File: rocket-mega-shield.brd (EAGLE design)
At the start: 114.3 x 60 mm, 57 parts

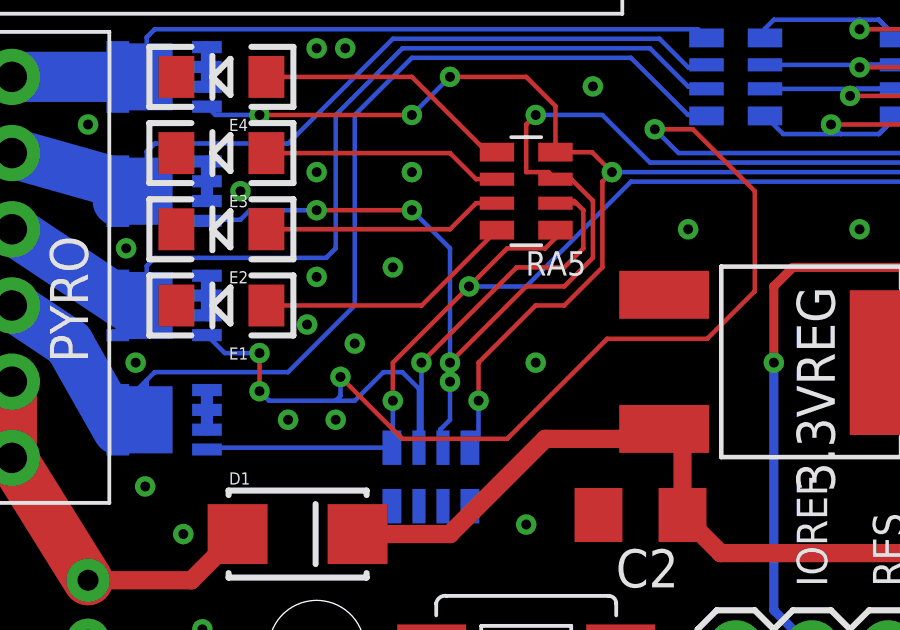
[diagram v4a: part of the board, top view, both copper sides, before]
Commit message: fixing goofy extra via
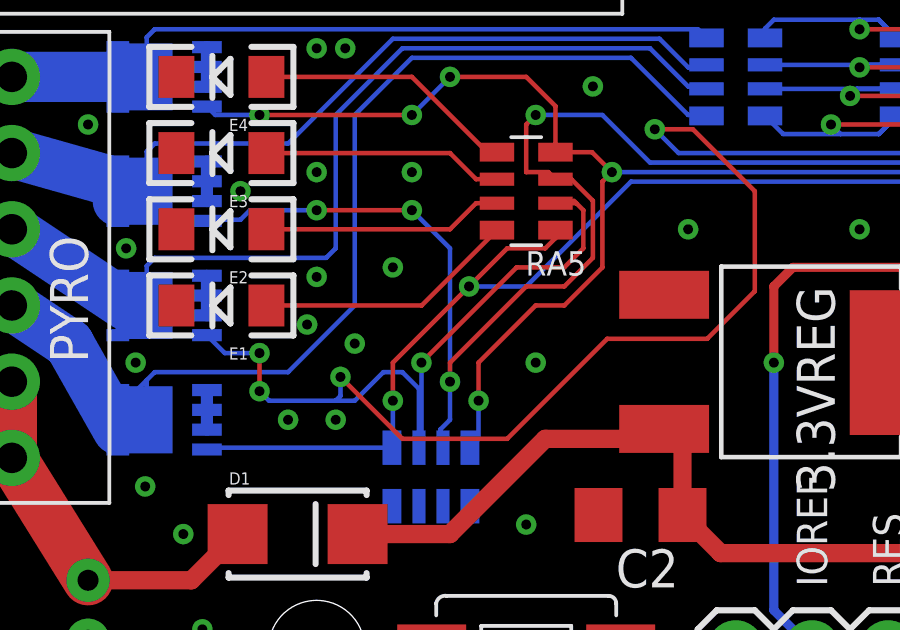
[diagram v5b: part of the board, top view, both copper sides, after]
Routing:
- net PYRO3: track 102.4 -> 103.0 mm, vias 5 -> 4
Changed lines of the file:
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@@
 <wire x1="26.9875" y1="13.6525" x2="26.9875" y2="13.1215" width="0.1524" layer="16"/>
 <wire x1="26.9875" y1="13.1215" x2="27.07" y2="13.039" width="0.1524" layer="16"/>
-<via x="27.305" y="15.875" extent="1-16" drill="0.3302"/>
-<wire x1="27.305" y1="15.875" x2="27.305" y2="19.685" width="0.1524" layer="16"/>
+<wire x1="27.305" y1="15.24" x2="27.305" y2="19.685" width="0.1524" layer="16"/>
 <wire x1="27.305" y1="19.685" x2="26.035" y2="20.955" width="0.1524" layer="16"/>
 <via x="26.035" y="20.955" extent="1-16" drill="0.3302"/>

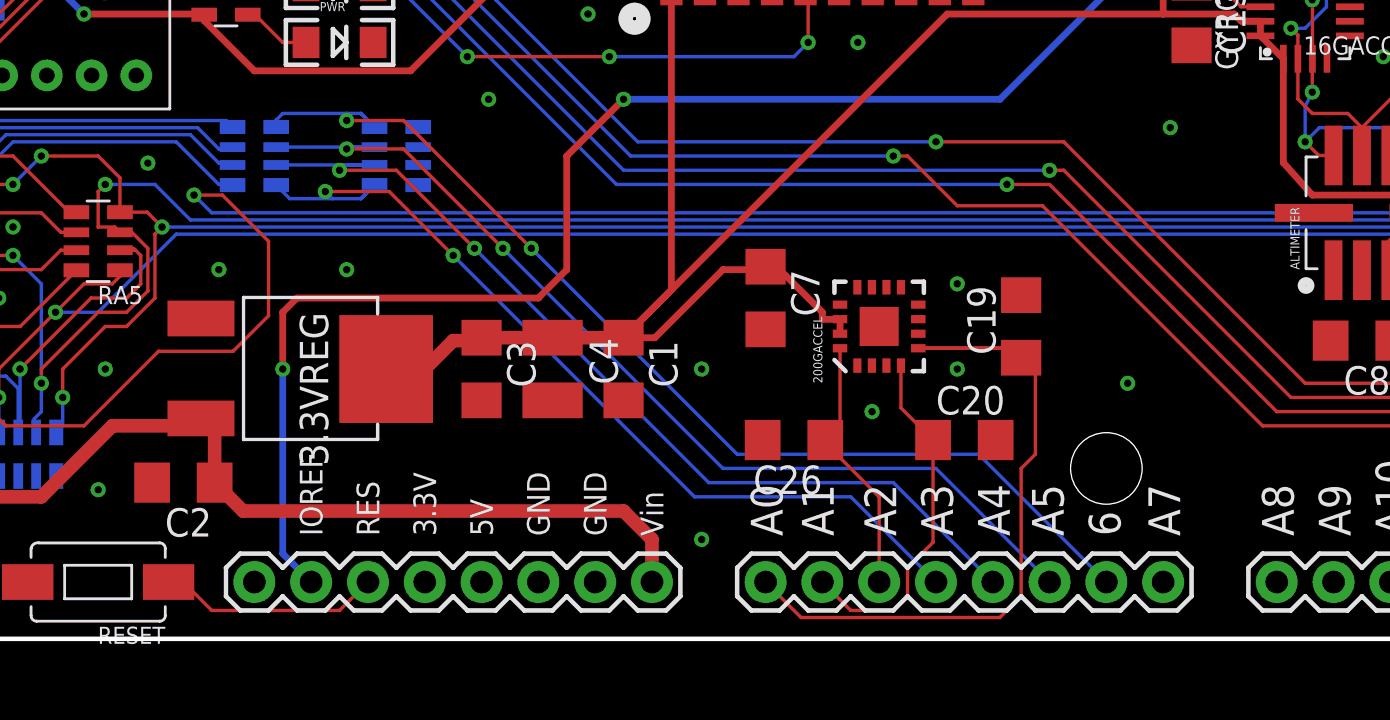
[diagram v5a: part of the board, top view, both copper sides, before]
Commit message: working on cleaning up the shield, will have to switch to the BMP180, went through the manifest and bill of materials
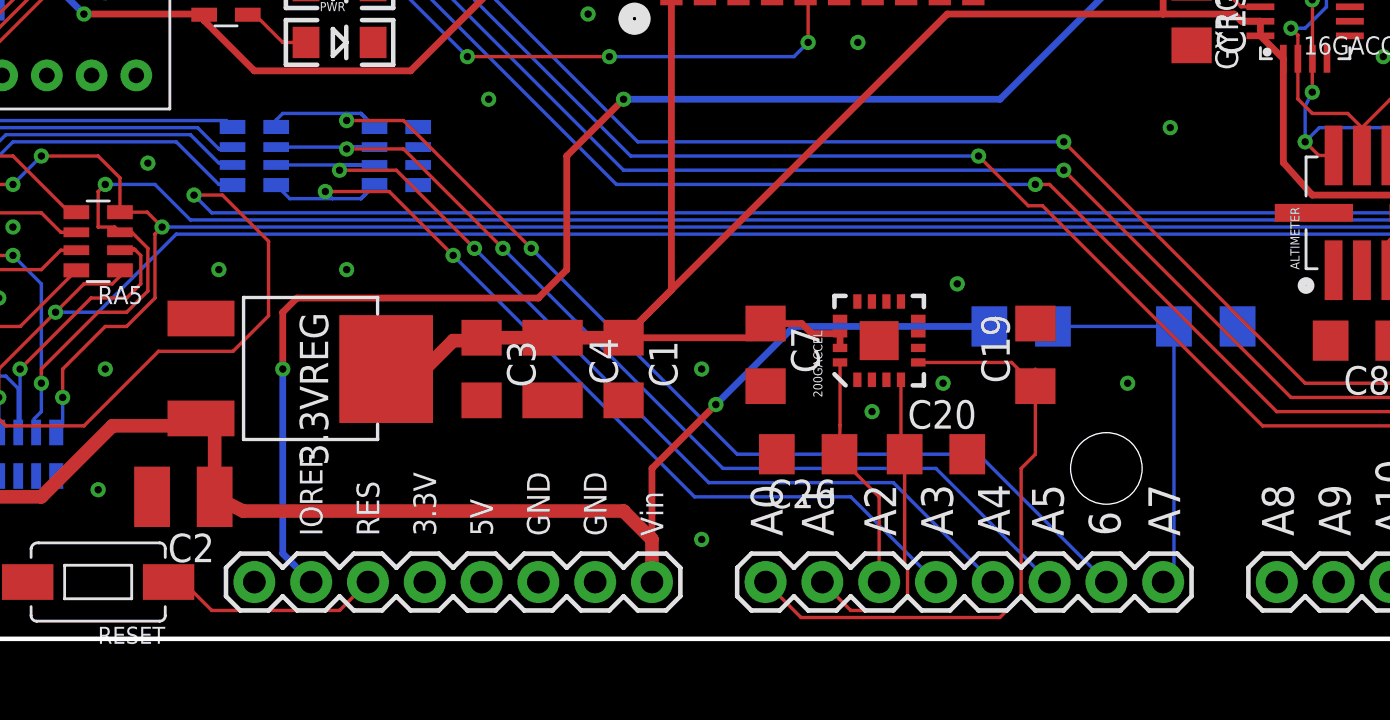
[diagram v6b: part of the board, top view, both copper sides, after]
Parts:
- added R1: 620k, adafruit:R1206
- added R2: 110k, adafruit:R1206
- C13: value 10nF -> 0.01uF
- C2: device adafruit:C1206 -> adafruit:C1210
- moved C7 2.54 mm to (59.7, 16.5)
- moved C20 1.42 mm to (67.3, 12.1)
- moved C19 1.42 mm to (71.8, 16.5)
- moved C26 0.90 mm to (61.6, 12.1)
- moved 200GACCEL 0.64 mm to (64.8, 17.1)
- moved C2 0.63 mm to (33.7, 10.2)
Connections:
- new net MEGAA7: MEGA.A7, R1.1, R2.2
- net GND: now also R2.1
- net VIN: now also R1.2
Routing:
- net VIN: track 37.3 -> 60.4 mm, vias 0 -> 1
- net MEGAA7: track 0.00 -> 17.0 mm
- net MEGAA0: track 33.3 -> 28.6 mm
- net MEGAA1: track 16.0 -> 14.4 mm
- net VCC3: track 276.3 -> 274.9 mm

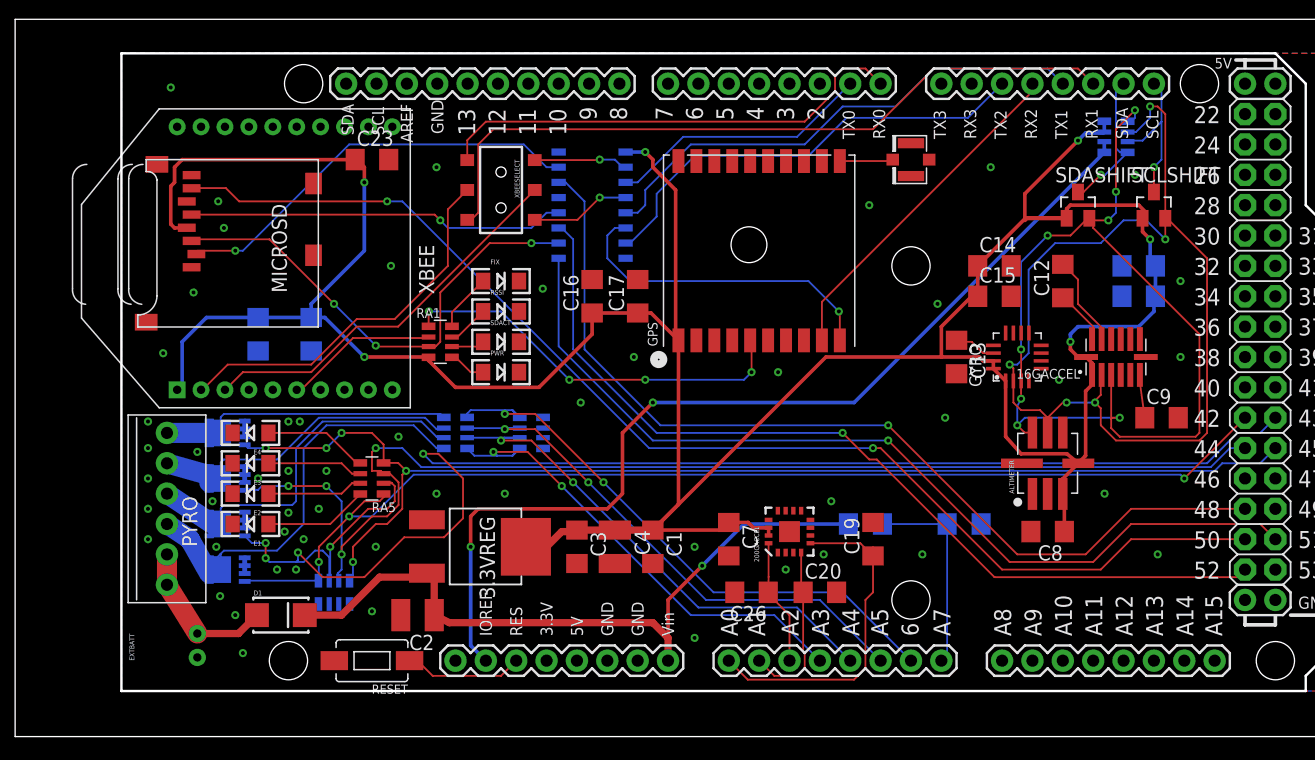
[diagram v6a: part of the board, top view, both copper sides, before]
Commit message: changed sd card, added holes to die down xb, changed reset switch, renamed all parts to match conventions, various other cleanup, adjusted BOM and manifest
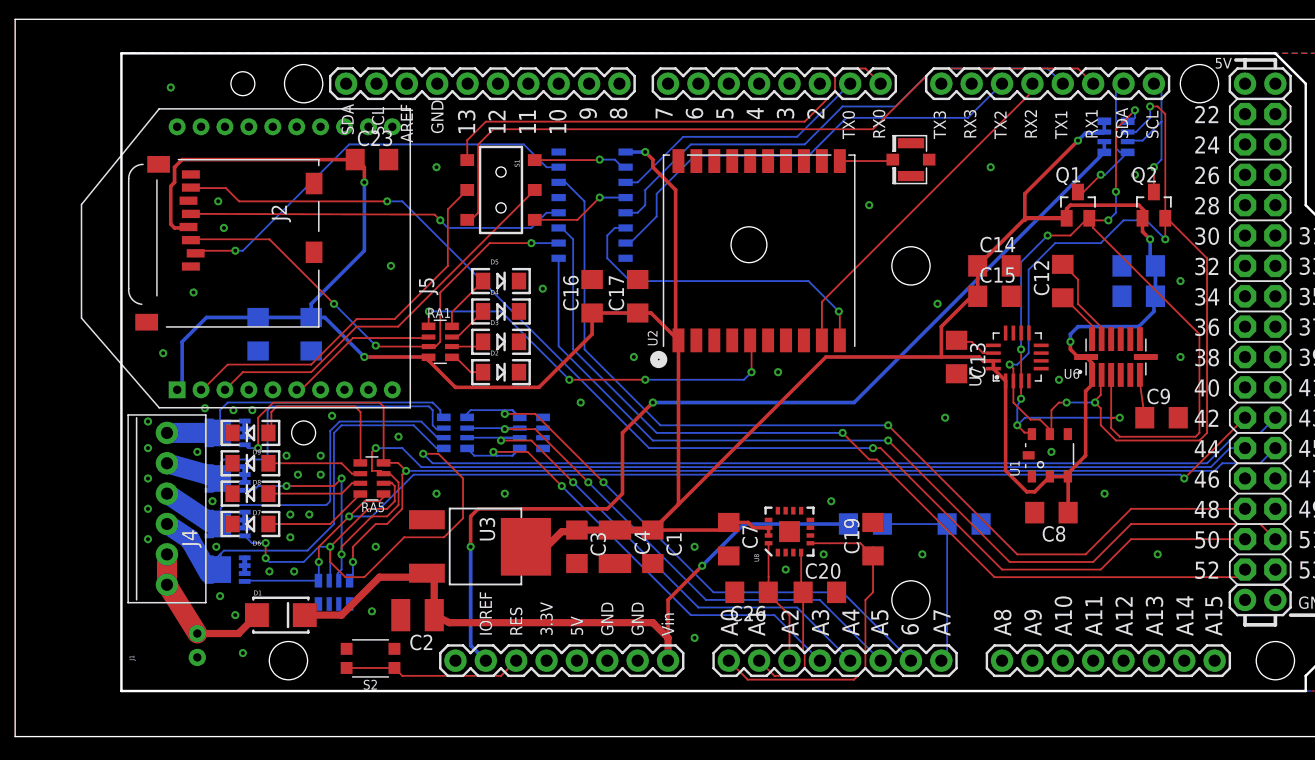
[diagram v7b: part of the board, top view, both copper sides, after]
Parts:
- removed ALTIMETER: BMP085, kurt:BMP085
- removed MICROSD: MICROSD, adafruit:MICROSD
- removed RESET: 1101NE, SparkFun-Electromechanical:TACTILE-SWITCH-1101NE
- added J2: MICROSD, zortness:MICROSD
- added S2: KMR2, zortness:TACTILE_KMR2
- added U1: BMP180, zortness:BMP180
- D2: value (none) -> PWR - green
- D3: value (none) -> SDAct - orange
- D4: value (none) -> RSSI - yellow
- D5: value (none) -> Fix - blue
- D6: value (none) -> Pyro1 - red
- D7: value (none) -> Pyro2 - red
- D8: value (none) -> Pyro3 - red
- D9: value (none) -> Pyro4 - red
- J1: value (none) -> ExtBatt
- J3: value ARDUINO-MEGAFULL -> Mega R3
- moved C8 1.62 mm to (86.7, 18.7)
- renumbered 16GACCEL to U6, 200GACCEL to U8, 3.3VREG to U3, CONV to U9, E1 to D6, E2 to D7, E3 to D8, E4 to D9, EXTBATT to J1, FIRST to Q3, FIX to D5, FOURTH to Q6, GPS to U2, GYRO to U7, MEGA to J3, PWR to D2, PYRO to J4, RSSI to D4, SCLSHIFT to Q2, SDACT to D3, SDASHIFT to Q1, SECOND to Q4, THIRD to Q5, XBEE to J5, XBEESELECT to S1
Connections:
- net GND: now also J2.6, J2.CD1, J2.CD2, J2.MT1, J2.MT2, S2.3, S2.4, U1.7; no longer ALTIMETER.P$1, MICROSD.6, MICROSD.CD1, MICROSD.CD2, MICROSD.MT1, MICROSD.MT2, RESET.P$2
- net MEGAMISO: now also J2.7; no longer MICROSD.7
- net MOSI: now also J2.3; no longer MICROSD.3
- net RESET: now also S2.1, S2.2; no longer RESET.P$1
- net SCL: now also U1.5; no longer ALTIMETER.P$6
- net SCLK: now also J2.5; no longer MICROSD.5
- net SDA: now also U1.6; no longer ALTIMETER.P$7
- net SDCS: now also J2.2; no longer MICROSD.2
- net VCC3: now also J2.4, U1.2, U1.3; no longer ALTIMETER.P$3, ALTIMETER.P$4, MICROSD.4
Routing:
- net N$16: track 8.72 -> 14.4 mm
- net PYRO4: track 102.0 -> 107.4 mm, vias 5 -> 3
- net RESET: track 9.97 -> 15.0 mm
- net PYRO2: track 121.8 -> 117.2 mm, vias 5 -> 4
- net N$25: track 29.7 -> 33.5 mm
- net PYRO3: track 103.0 -> 104.7 mm
- net N$24: track 29.8 -> 31.2 mm
- net SCL: track 84.3 -> 85.7 mm
- net N$4: track 33.8 -> 34.7 mm
- net VCC3: track 274.9 -> 275.7 mm
- net N$3: track 37.6 -> 38.4 mm
- net GND: vias 52 -> 55

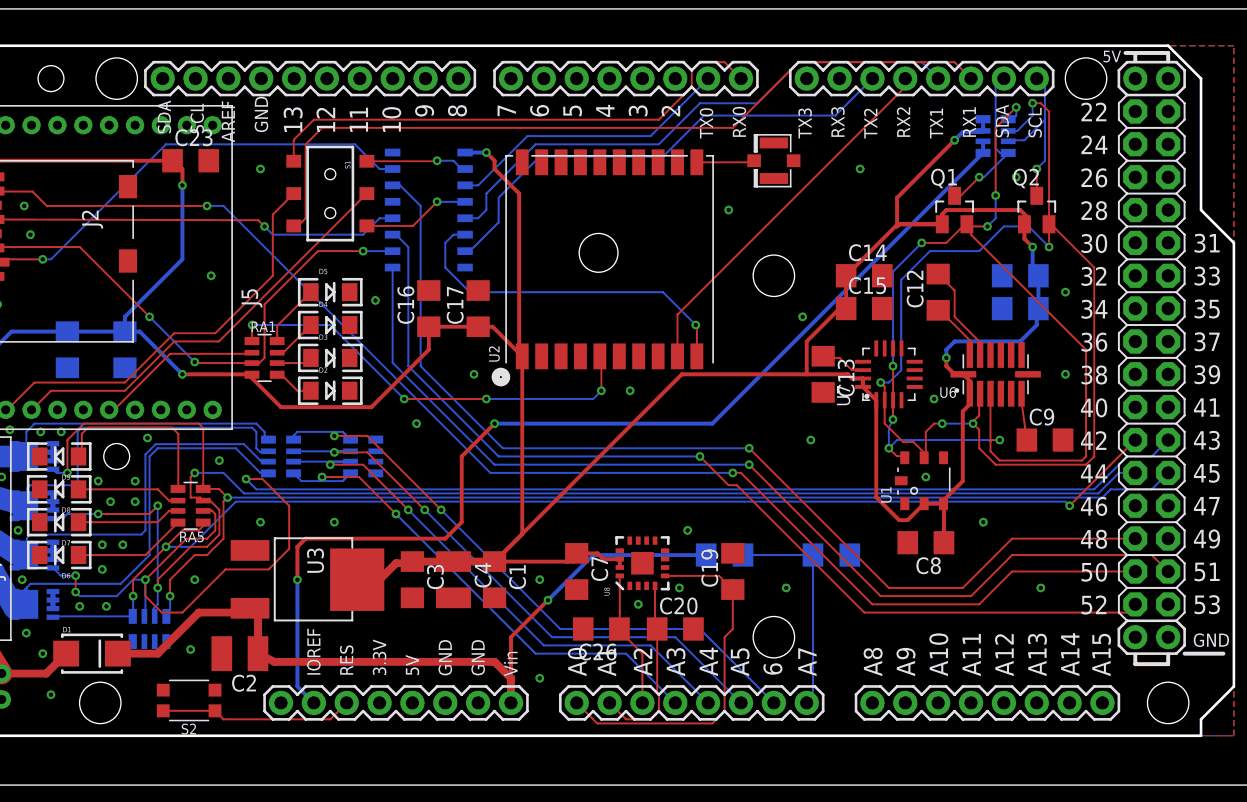
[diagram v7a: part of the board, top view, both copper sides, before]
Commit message: added buzzer on pin 8, moved all analog reads down to second set of pins, A8-A15, updated manifest, bom, and images
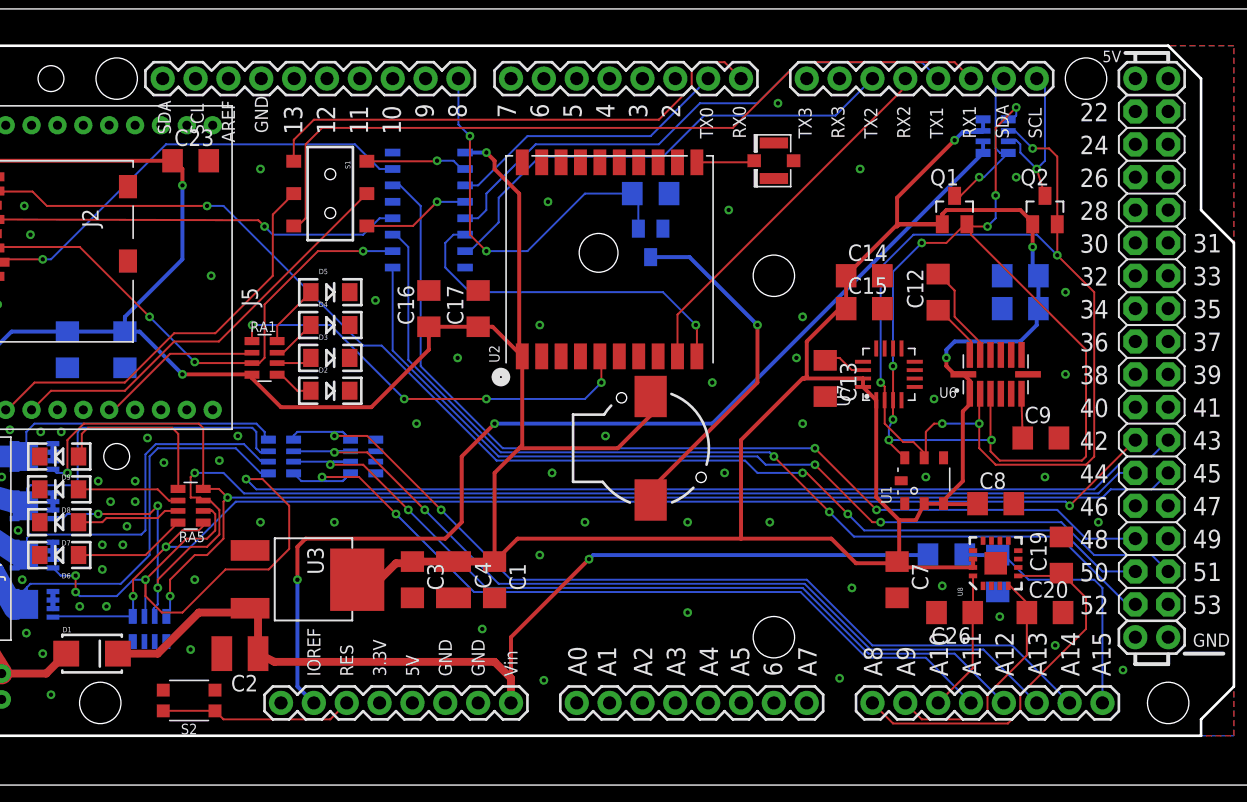
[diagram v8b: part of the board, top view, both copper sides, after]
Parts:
- added Q7: BSS138, kurt:SOT23
- added R3: 10k, adafruit:R1206
- added SG1: CCV084, SparkFun-Electromechanical:BUZZER-CCV
- moved C20 28.6 mm to (95.9, 13.3)
- moved C26 27.3 mm to (88.9, 13.3)
- moved U8 27.3 mm to (92.1, 17.1)
- moved C19 25.4 mm to (97.2, 17.8)
- moved C7 24.8 mm to (84.5, 15.9)
- moved R1 17.1 mm to (88.3, 17.8)
- moved R2 12.9 mm to (92.2, 16.4), turned to 90 degrees
- moved C8 6.18 mm to (92.1, 21.7), turned to 0 degrees
- moved Q2 0.64 mm to (95.9, 44.5)
- moved C9 0.35 mm to (95.6, 26.8)
- moved C13 0.35 mm to (78.9, 31.4)
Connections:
- new net MEGA8: J3.8, Q7.1, R3.1
- new net MEGAA10: C26.1, J3.A10, U8.16
- new net MEGAA11: J3.A11, RA3.4, RA4.5
- new net MEGAA12: J3.A12, RA3.3, RA4.6
- new net MEGAA13: J3.A13, RA3.2, RA4.7
- new net MEGAA14: J3.A14, RA3.1, RA4.8
- new net MEGAA15: J3.A15, R1.1, R2.2
- new net MEGAA8: C19.1, J3.A8, U8.5
- new net MEGAA9: C20.1, J3.A9, U8.4
- new net N$13: Q7.3, SG1.+
- net GND: now also Q7.2, R3.2
- net MEGAA0: no longer C19.1, U8.5
- net MEGAA1: no longer C20.1, U8.4
- net MEGAA2: no longer C26.1, U8.16
- net MEGAA3: no longer RA3.4, RA4.5
- net MEGAA4: no longer RA3.3, RA4.6
- net MEGAA5: no longer RA3.2, RA4.7
- net MEGAA6: no longer RA3.1, RA4.8
- net MEGAA7: no longer R1.1, R2.2
- net VCC3: now also SG1.-
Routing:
- net MEGAA14: track 0.00 -> 71.6 mm, vias 0 -> 2
- net MEGAA13: track 0.00 -> 68.0 mm, vias 0 -> 2
- net MEGAA12: track 0.00 -> 65.8 mm, vias 0 -> 2
- net MEGAA11: track 0.00 -> 63.9 mm, vias 0 -> 2
- net MEGAA6: track 48.8 -> 0.00 mm, vias 2 -> 0
- net MEGAA5: track 45.1 -> 0.00 mm, vias 2 -> 0
- net MEGAA4: track 42.9 -> 0.00 mm, vias 2 -> 0
- net MEGAA3: track 41.1 -> 0.00 mm, vias 2 -> 0
- net MEGA8: track 0.00 -> 30.3 mm, vias 0 -> 2
- net MEGAA8: track 0.00 -> 29.5 mm
- net MEGAA0: track 28.6 -> 0.00 mm
- net N$13: track 0.00 -> 28.2 mm, vias 0 -> 1
- net VCC3: track 275.7 -> 303.9 mm
- net MEGAA15: track 0.00 -> 20.6 mm
- net MEGAA9: track 0.00 -> 19.0 mm
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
